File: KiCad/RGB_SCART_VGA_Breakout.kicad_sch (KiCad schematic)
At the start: 23 parts, among them J1 SCART-F, J11 SJ1-3535NG, J3 DE15_Plug_HighDensity_Mountin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, J4 Conn_01x09, J5 Mounting, J6 Mounting, J7 Mounting, J8 Mounting

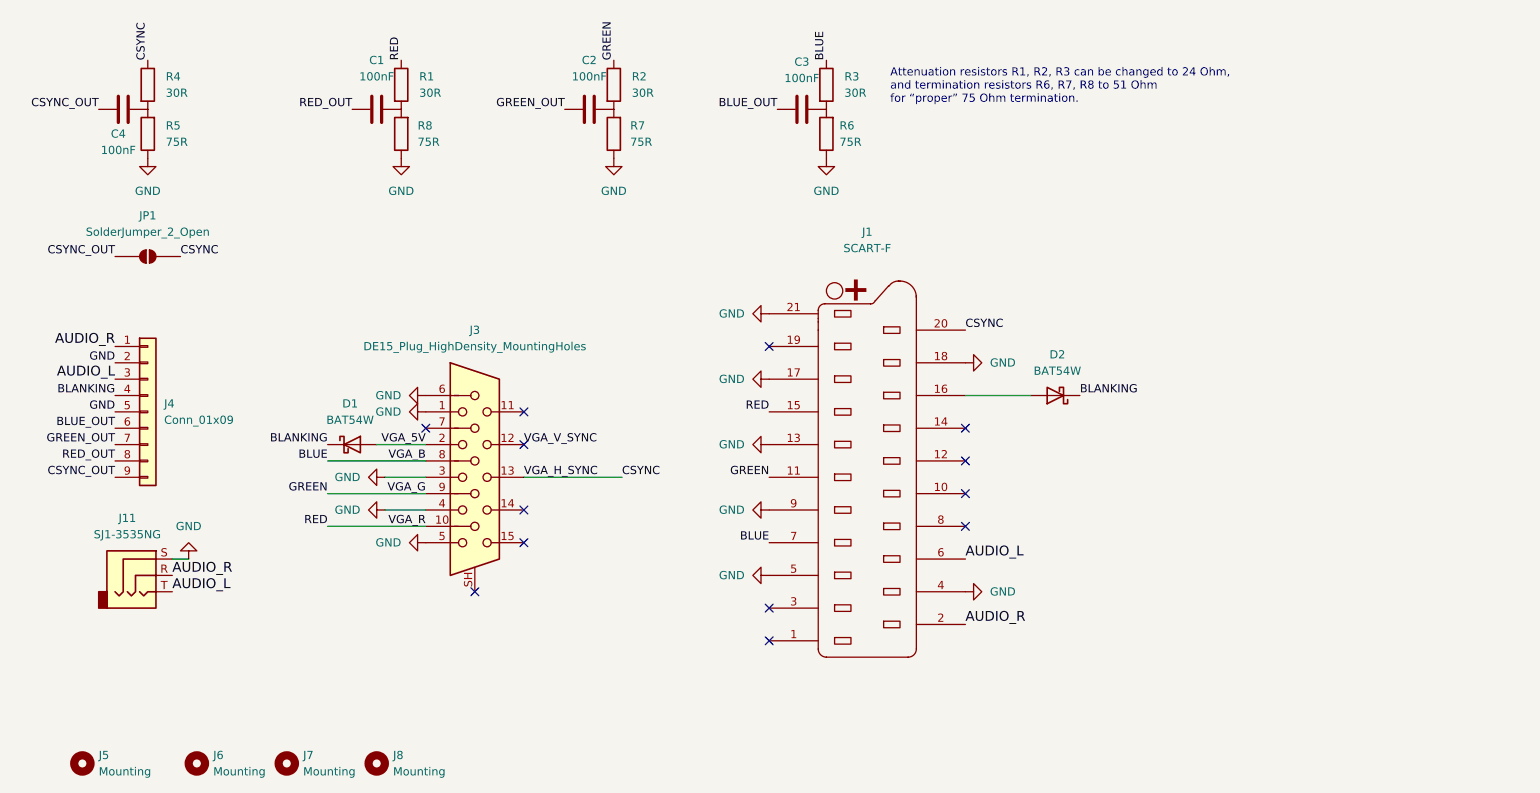
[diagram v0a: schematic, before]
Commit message: Fixed DE15/VGA connector pinout.
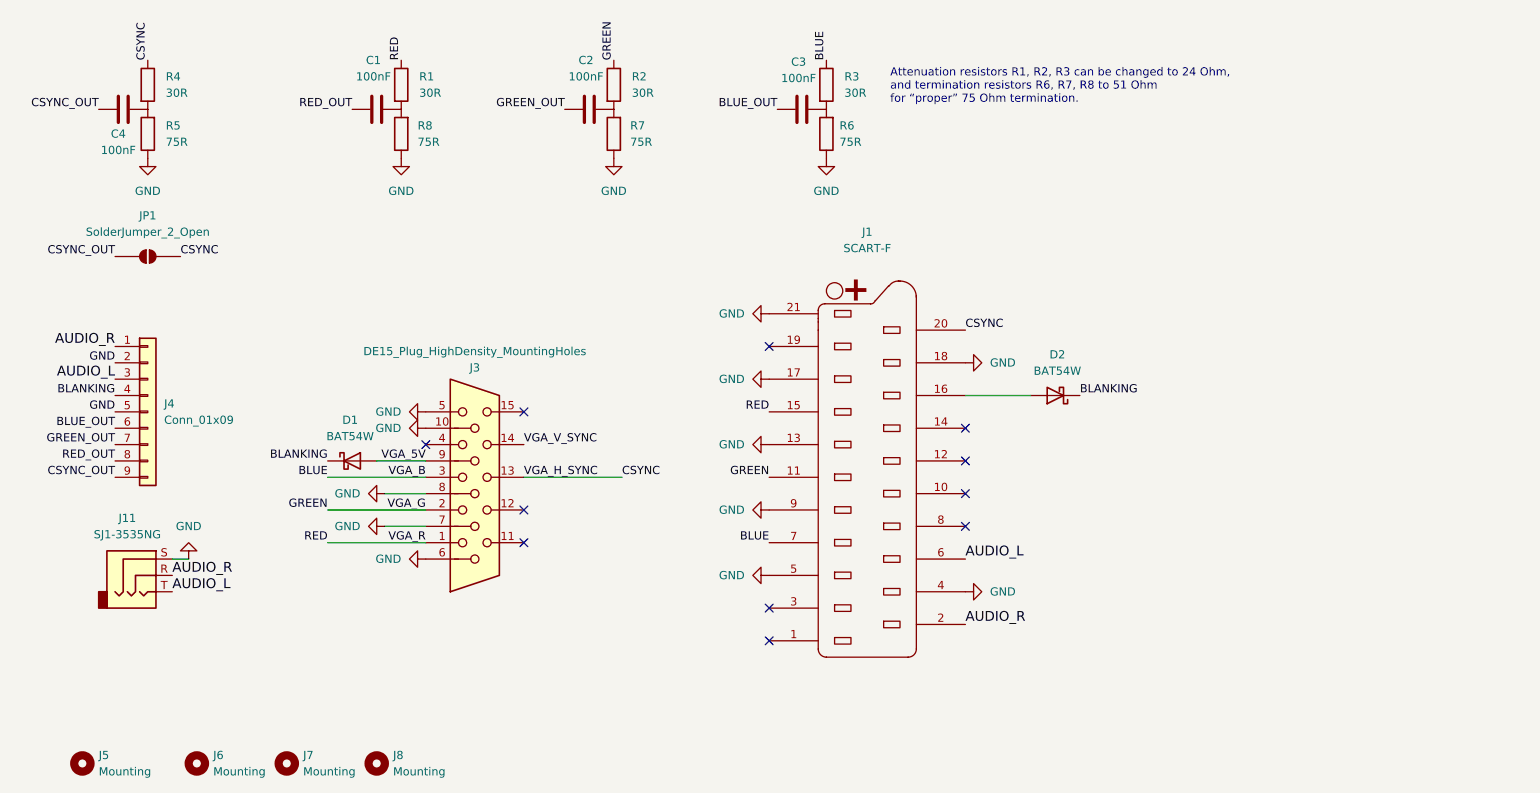
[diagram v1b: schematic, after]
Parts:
- J3: symbol Connector:DE15_Socket_HighDensity_MountingHoles -> Connector:DE15_Socket_HighDensity
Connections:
- net BLUE: now also J3.3; no longer J3.8
- net GND: now also J3.10, J3.7, J3.8; no longer J3.1, J3.3, J3.4
- net GREEN: now also J3.2; no longer J3.9
- net RED: now also J3.1; no longer J3.10
- net VGA_5V: now also J3.9; no longer J3.2
- net VGA_V_SYNC: now also J3.14; no longer J3.12
- no-connect marks 13 -> 11
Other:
- moved on the sheet: D1

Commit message: Added blanking voltage divider / pulldown resistors with description. Expanded RGB load / voltage divider resistors description. VGA pins 7,8,10 connected to GND.
PCB version 1.1.
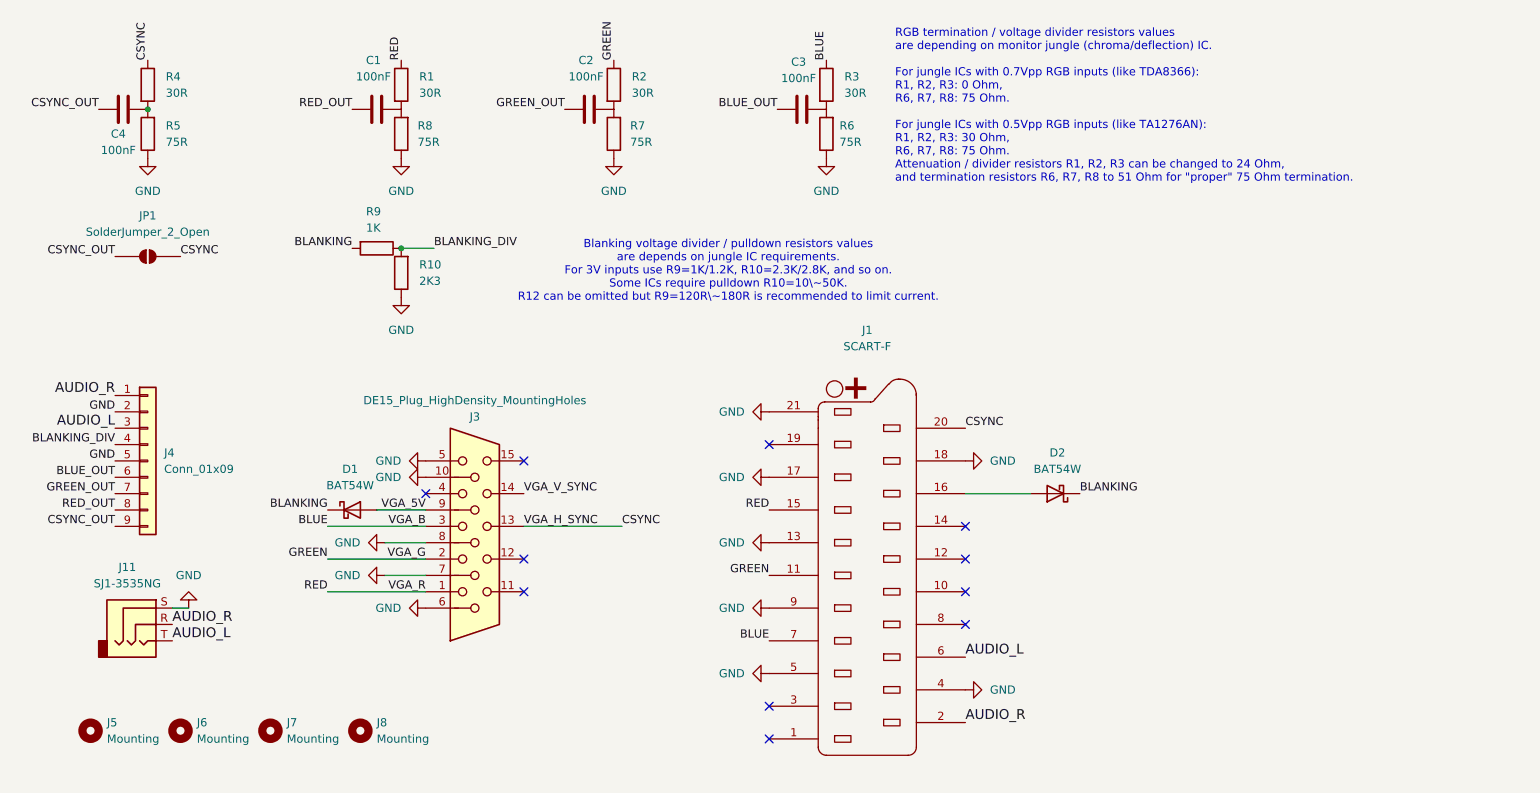
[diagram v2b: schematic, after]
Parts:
- added R10: 2K3, Resistor_SMD:R_0805_2012Metric, symbol Device:R
- added R9: 1K, Resistor_SMD:R_0805_2012Metric, symbol Device:R
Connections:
- net BLANKING: now also R9.2; no longer J4.4 (Pin_4)
- net GND: now also R10.1
- new net BLANKING_DIV: J4.4 (Pin_4), R10.2, R9.1
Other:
- note added: "Blanking voltage divider / pulldown resistors values are depends on jungle IC requirements. For 3V inputs use R9=1K/1.2K, R10=2.3K/2.8K, and so on. Some ICs require pulldown R10=10\~50K. R12 can be omitted but R9=120R\~180R is recommended to limit current."
- note added: "RGB termination / voltage divider resistors values are depending on monitor jungle (chroma/deflection) IC. For jungle ICs with 0.7Vpp RGB inputs (like TDA8366): R1, R2, R3: 0 Ohm, R6, R7, R8: 75 Ohm. For jungle ICs with 0.5Vpp RGB inputs (like TA1276AN): R1, R2, R3: 30 Ohm, R6, R7, R8: 75 Ohm. Attenuation / divider resistors R1, R2, R3 can be changed to 24 Ohm, and termination resistors R6, R7, R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"
- note removed: "Attenuation resistors R1, R2, R3 can be changed to 24 Ohm, and termination resistors R6, R7, R8 to 51 Ohm for “proper” 75 Ohm termination."
- moved on the sheet: D1, D2, J1, J11, J3, J4, J5, J6, J7, J8
